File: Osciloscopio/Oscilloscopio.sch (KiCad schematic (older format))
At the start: 0 parts

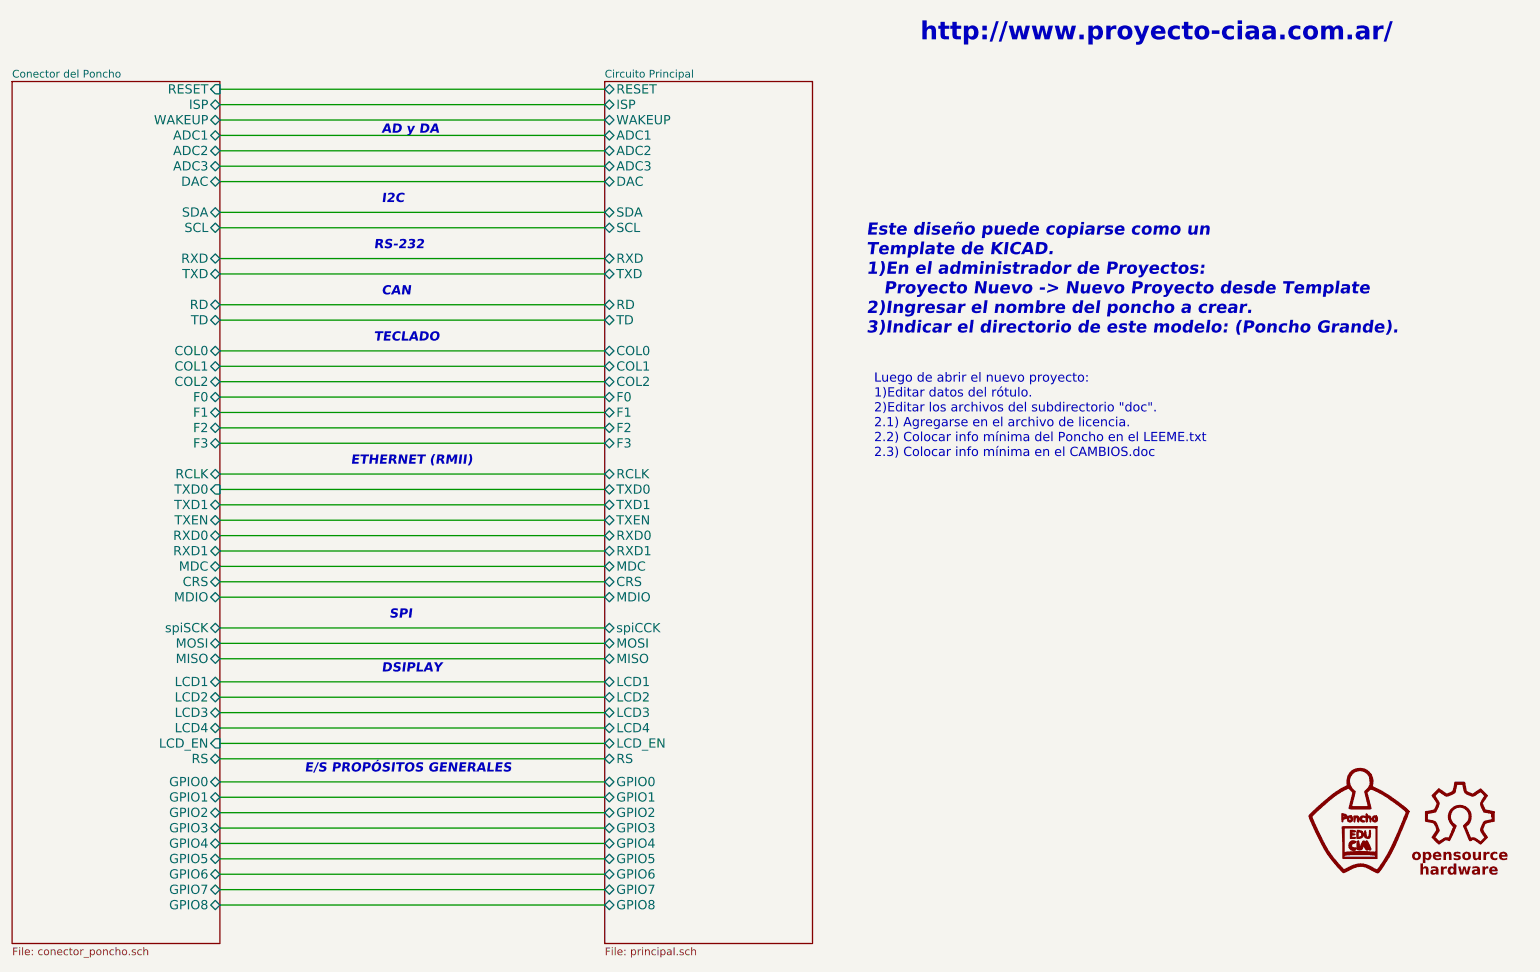
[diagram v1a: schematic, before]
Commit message: Se finalizan las correciones sugeridas a nivel esquematico
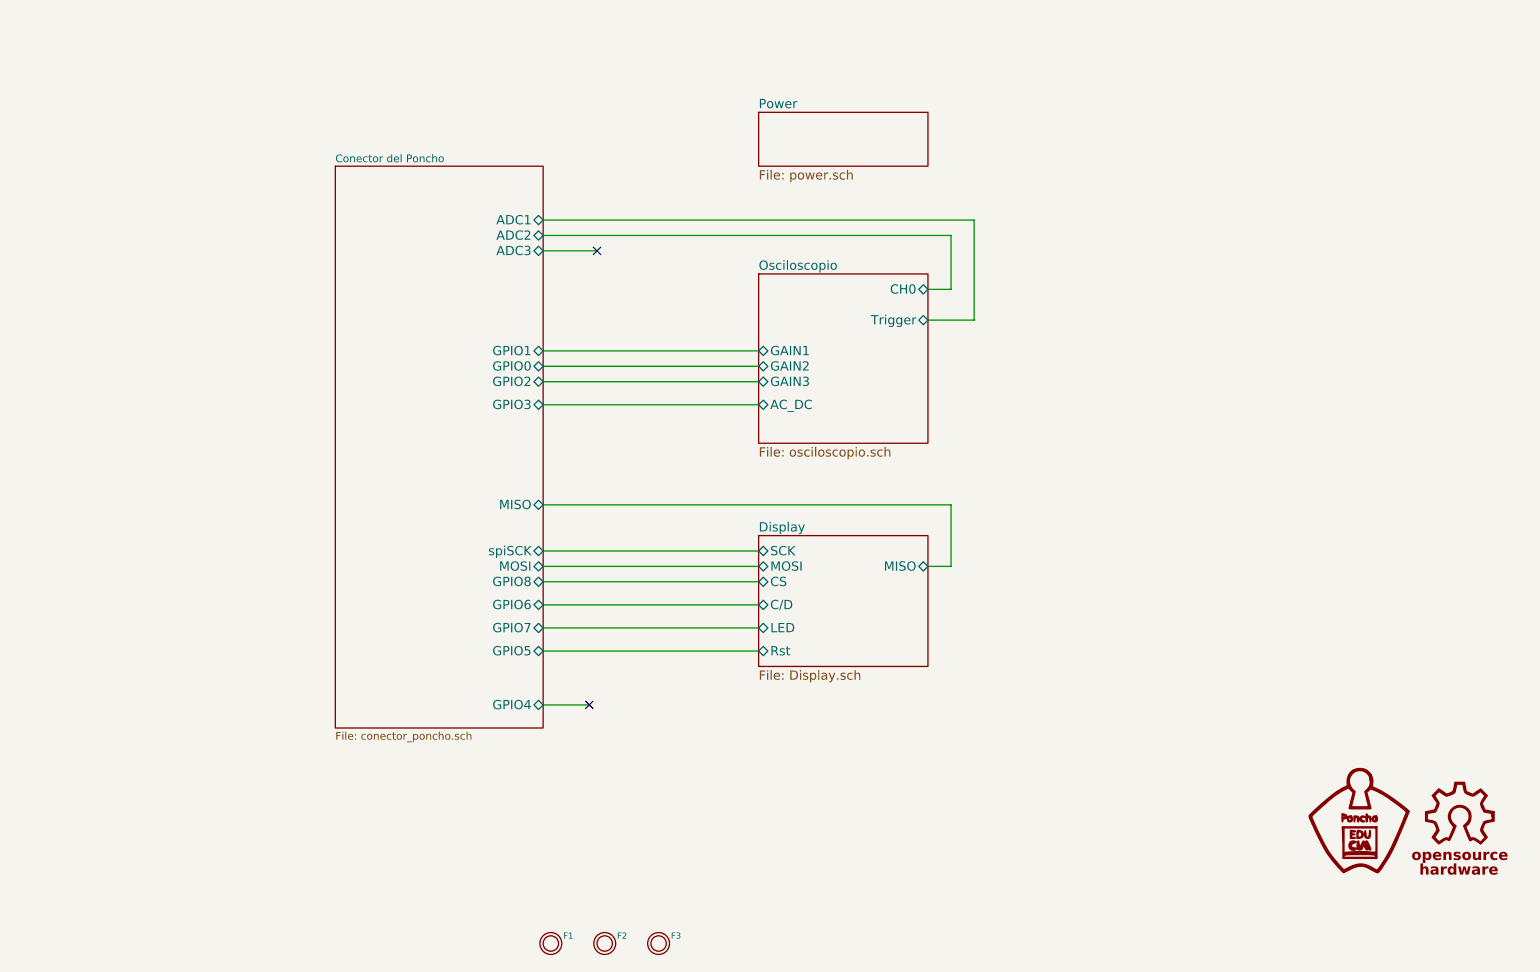
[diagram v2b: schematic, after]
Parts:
- added F1, F2, F3: FIDUCIAL, osc:Fiducial_1mm, symbol FIDUCIAL
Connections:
- no-connect marks 0 -> 2
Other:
- note removed: "AD y DA"
- note removed: "CAN"
- note removed: "DSIPLAY"
- note removed: "E/S PROPÓSITOS GENERALES"
- note removed: "ETHERNET (RMII)"
- note removed: "Este diseño puede copiarse como un \nTemplate de KICAD. \n1)En el administrador de Proyectos: \n Proyecto Nuevo -> Nuevo Proyecto desde Template\n2)Ingresar el nombre del poncho a crear.\n3)Indicar el directorio de este modelo: (Poncho Grande)."
- note removed: "I2C"
- note removed: "Luego de abrir el nuevo proyecto:\n1)Editar datos del rótulo.\n2)Editar los archivos del subdirectorio "doc".\n2.1) Agregarse en el archivo de licencia.\n2.2) Colocar info mínima del Poncho en el LEEME.txt\n2.3) Colocar info mínima en el CAMBIOS.doc"
- note removed: "RS-232"
- note removed: "SPI"
- note removed: "TECLADO"
- note removed: "http://www.proyecto-ciaa.com.ar/"

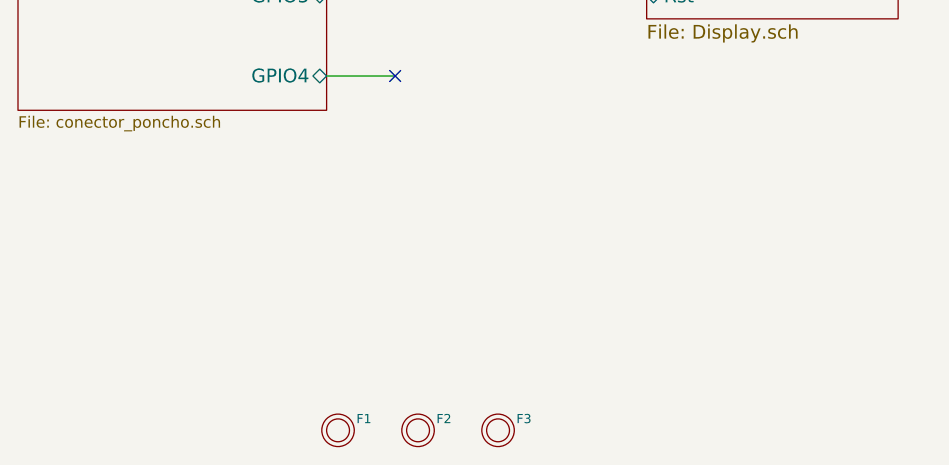
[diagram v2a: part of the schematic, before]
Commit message: Corrección cod. digikey del conector de poncho osciloscopio, aclaración sobre zócalos para los dip.
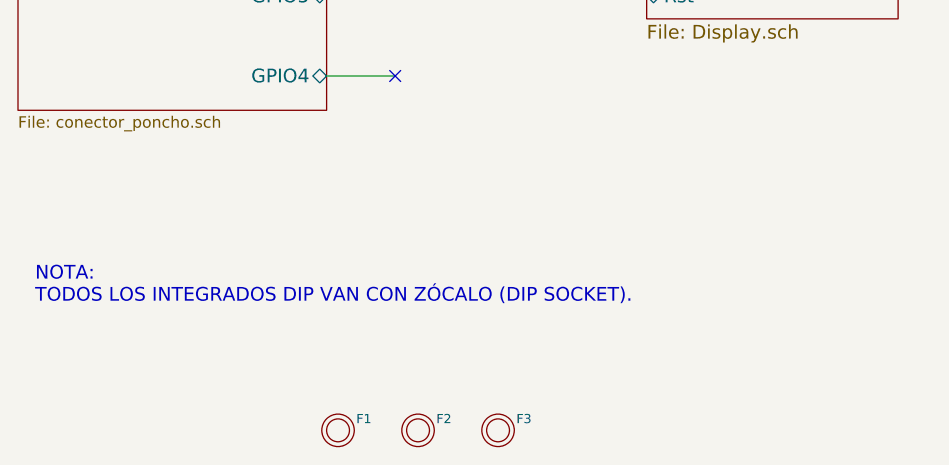
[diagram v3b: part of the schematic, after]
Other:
- note added: "NOTA:\nTODOS LOS INTEGRADOS DIP VAN CON ZÓCALO (DIP SOCKET)."
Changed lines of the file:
@@
 Wire Wire Line
 	7350 2750 7650 2750
+Text Notes 3575 6250 0    60   ~ 0
+NOTA:\nTODOS LOS INTEGRADOS DIP VAN CON ZÓCALO (DIP SOCKET).
 $EndSCHEMATC
